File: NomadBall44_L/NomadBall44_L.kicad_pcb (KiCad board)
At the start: 2 copper layers, 149 x 203 mm, 58 parts, among them SW1 SW_Push, SW10 SW_Push, SW11 SW_Push, SW12 SW_Push, SW13 SW_Push, SW14 SW_Push, SW15 SW_Push, SW16 SW_Push, SW17 SW_Push, SW18 SW_Push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

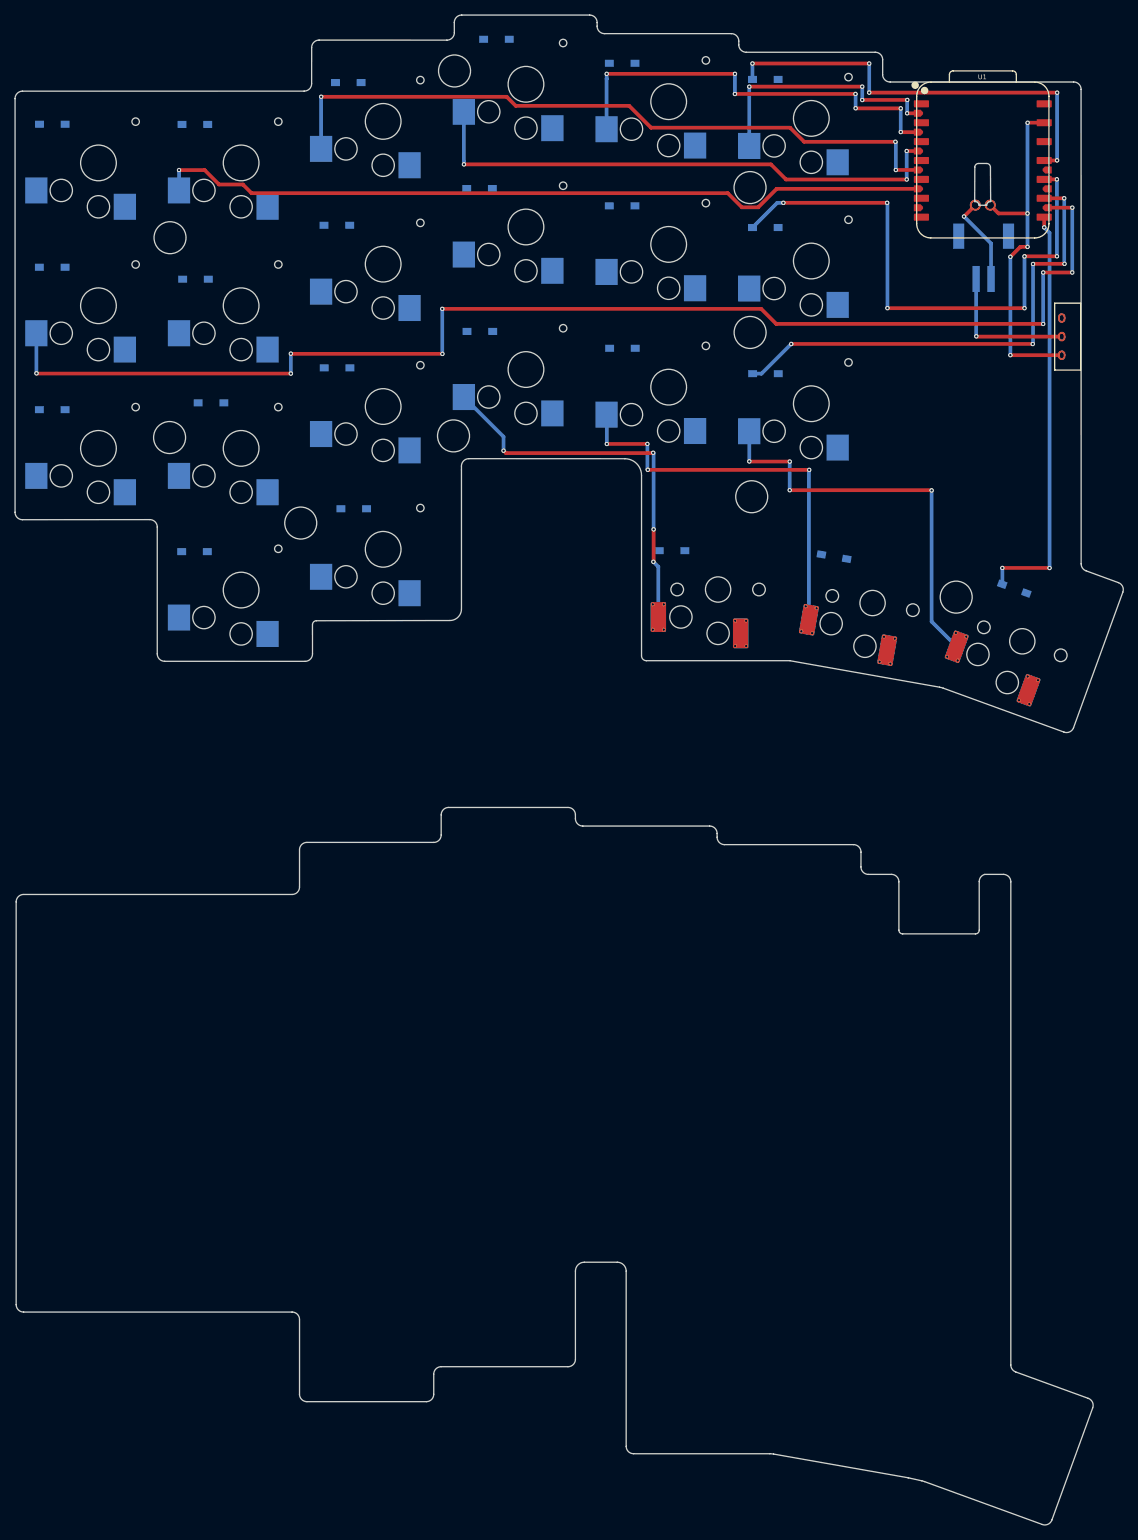
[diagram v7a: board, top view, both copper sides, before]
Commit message: キースイッチの配線が完了
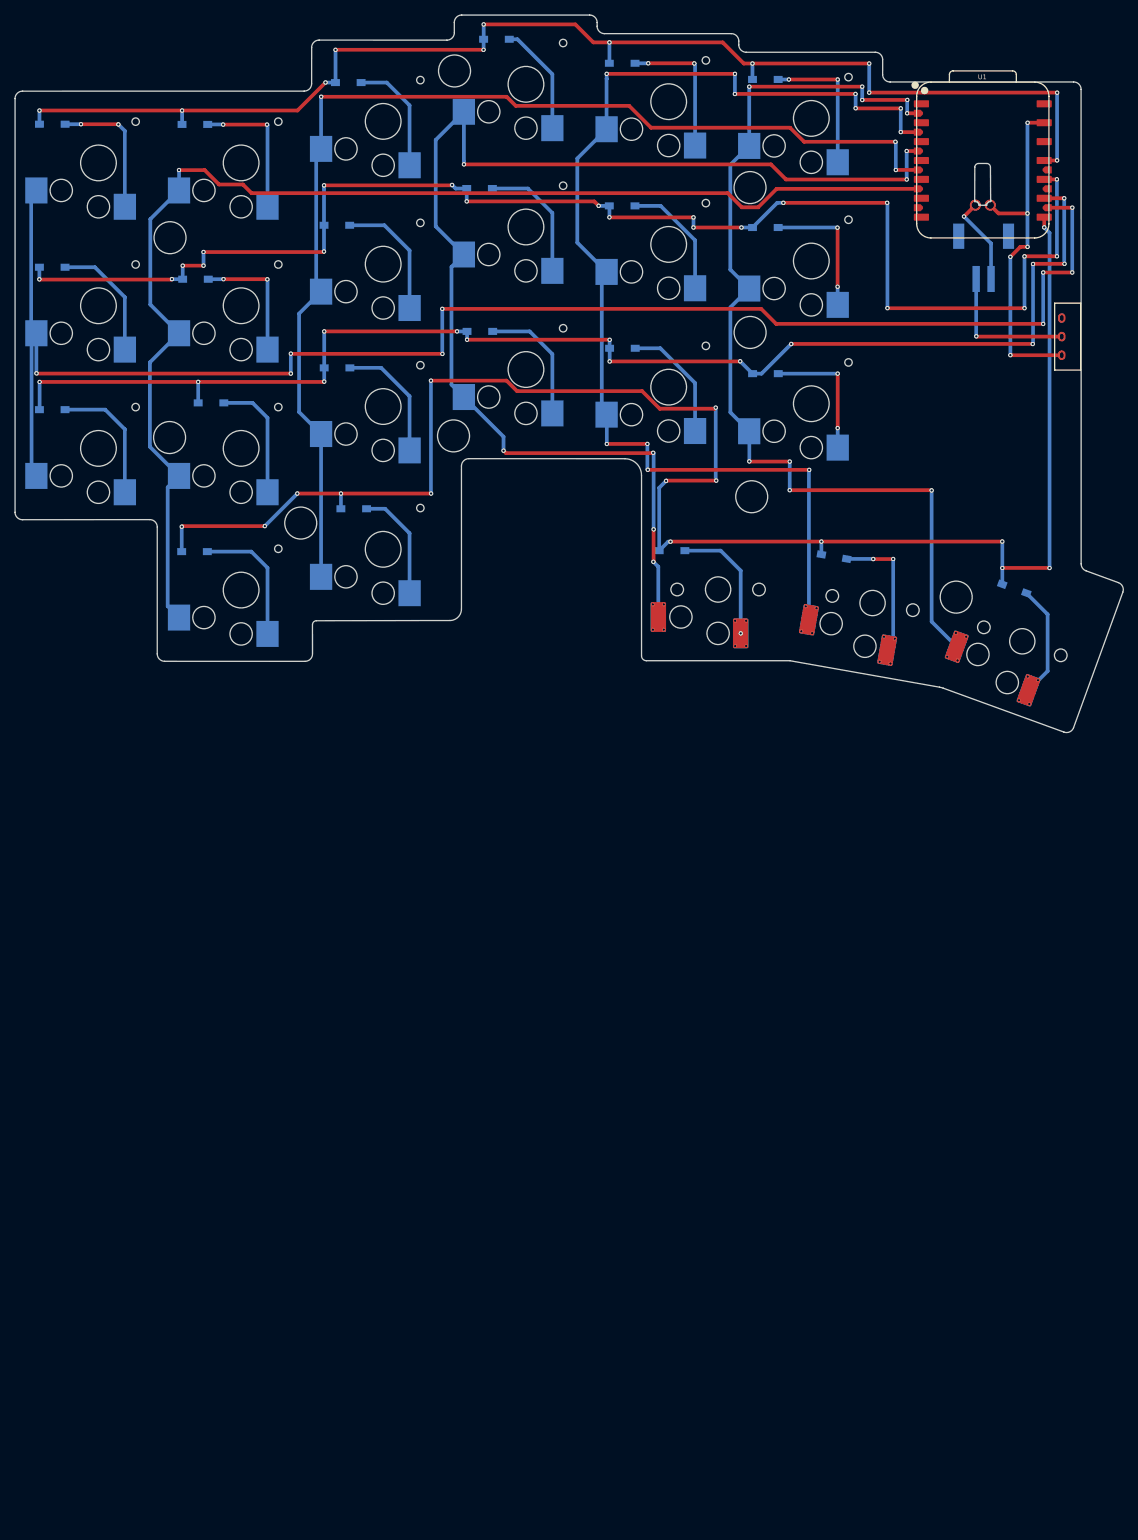
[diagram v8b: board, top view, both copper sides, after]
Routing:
- net Row3: track 56.0 -> 230.2 mm, vias 3 -> 15
- net Row1: track 75.5 -> 190.7 mm, vias 7 -> 21
- net Row0: track 57.9 -> 171.8 mm, vias 5 -> 12
- net Row2: track 65.8 -> 179.8 mm, vias 5 -> 14
- net Col4: track 105.3 -> 170.4 mm
- net Col3: track 93.6 -> 154.1 mm
- net Col2: track 124.9 -> 167.8 mm
- net Col0: track 89.2 -> 131.7 mm
- net Col1: track 111.9 -> 154.1 mm
- net Col5: track 173.3 -> 212.8 mm
- net Net-(D1-A): track 0.00 -> 19.1 mm, vias 0 -> 2
- net Net-(D5-A): track 0.00 -> 19.1 mm, vias 0 -> 2
- net Net-(D2-A): track 0.00 -> 19.1 mm, vias 0 -> 2
- net Net-(D20-A): track 0.00 -> 18.8 mm, vias 0 -> 2
- net Net-(D6-A): track 0.00 -> 18.6 mm, vias 0 -> 2
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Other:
- board size 149 x 203 mm -> 149 x 96.5 mm
